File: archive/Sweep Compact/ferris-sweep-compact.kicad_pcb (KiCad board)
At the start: 2 copper layers, 107.2 x 86.9 mm, 21 parts, among them J1 MJ-4PP-9, SW10 SW_PUSH, SW11 SW_PUSH, SW12 SW_PUSH, SW14 SW_PUSH, SW15 SW_PUSH, SW16 SW_PUSH, SW17 SW_PUSH, SW18 SW_PUSH, SW2 SW_PUSH, SW20 SW_PUSH, SW21 SW_PUSH, SW3 SW_PUSH, SW4 SW_PUSH, SW5 SW_PUSH, SW6 SW_PUSH, SW8 SW_PUSH, SW9 SW_PUSH, U1 ProMicro

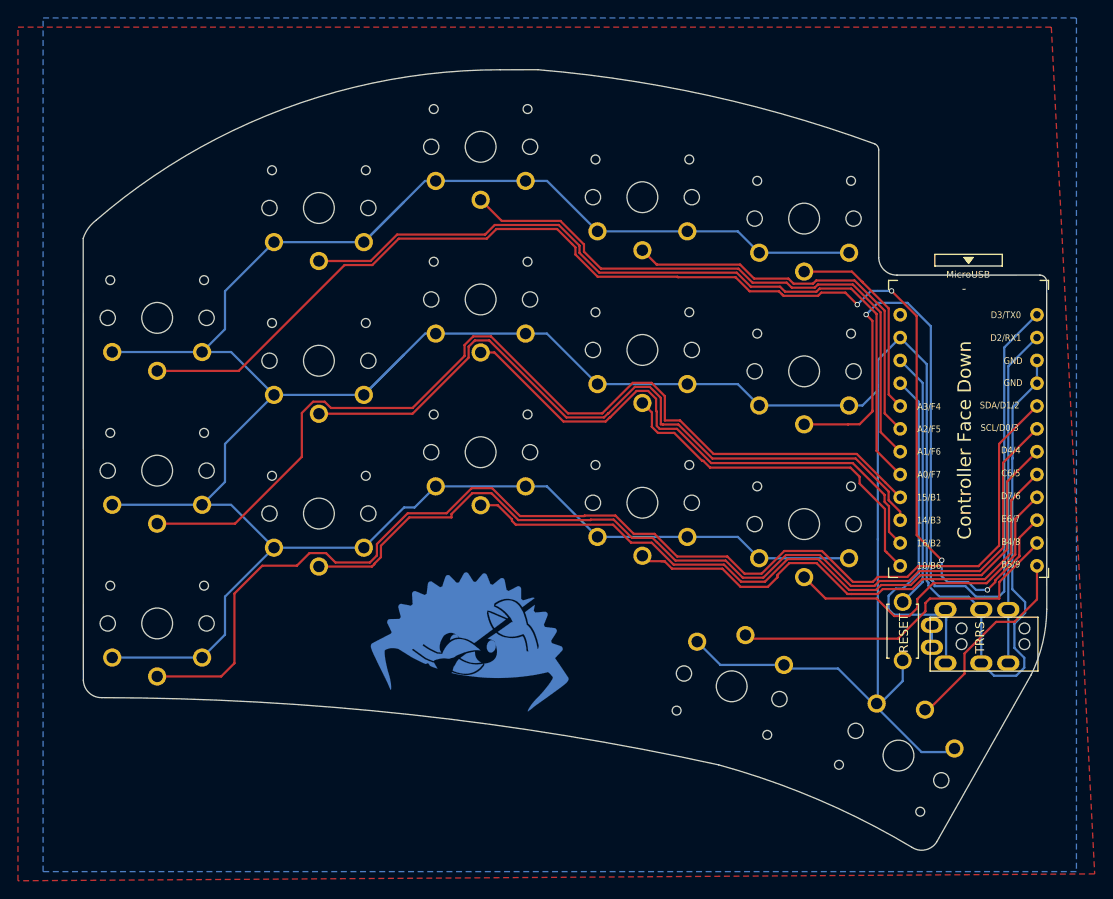
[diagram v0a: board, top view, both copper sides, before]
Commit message: feat: adjust cutout shape of sweep compact
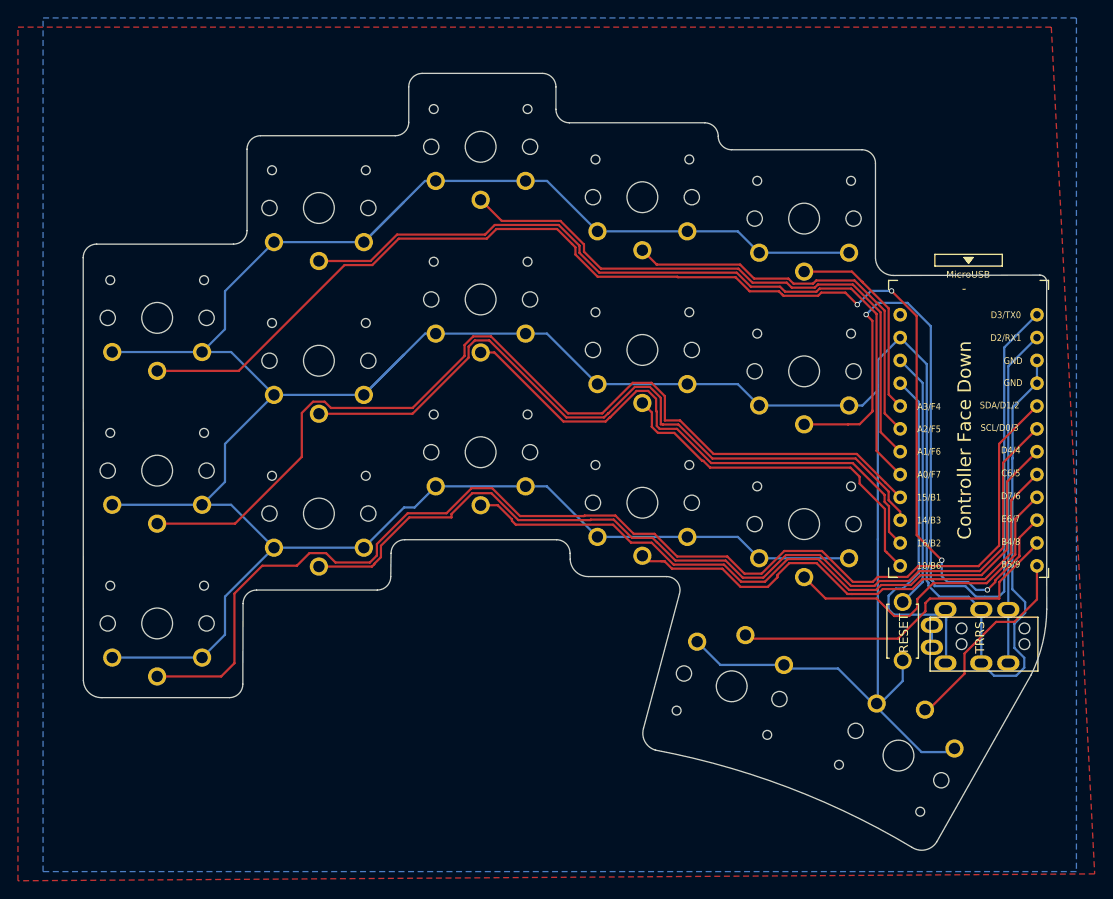
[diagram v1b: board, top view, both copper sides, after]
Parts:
- removed G***: LOGO, Kailh:ferris_broom
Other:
- board size 107.2 x 86.9 mm -> 107.2 x 86.5 mm
- net class Default removed
